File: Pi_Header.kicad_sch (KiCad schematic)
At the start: 31 parts, among them J1 Raspberry_Pi_2_3, J2 UART, J3 I2C, J4 Power_IN, U1 BD9F800MUX-ZE2

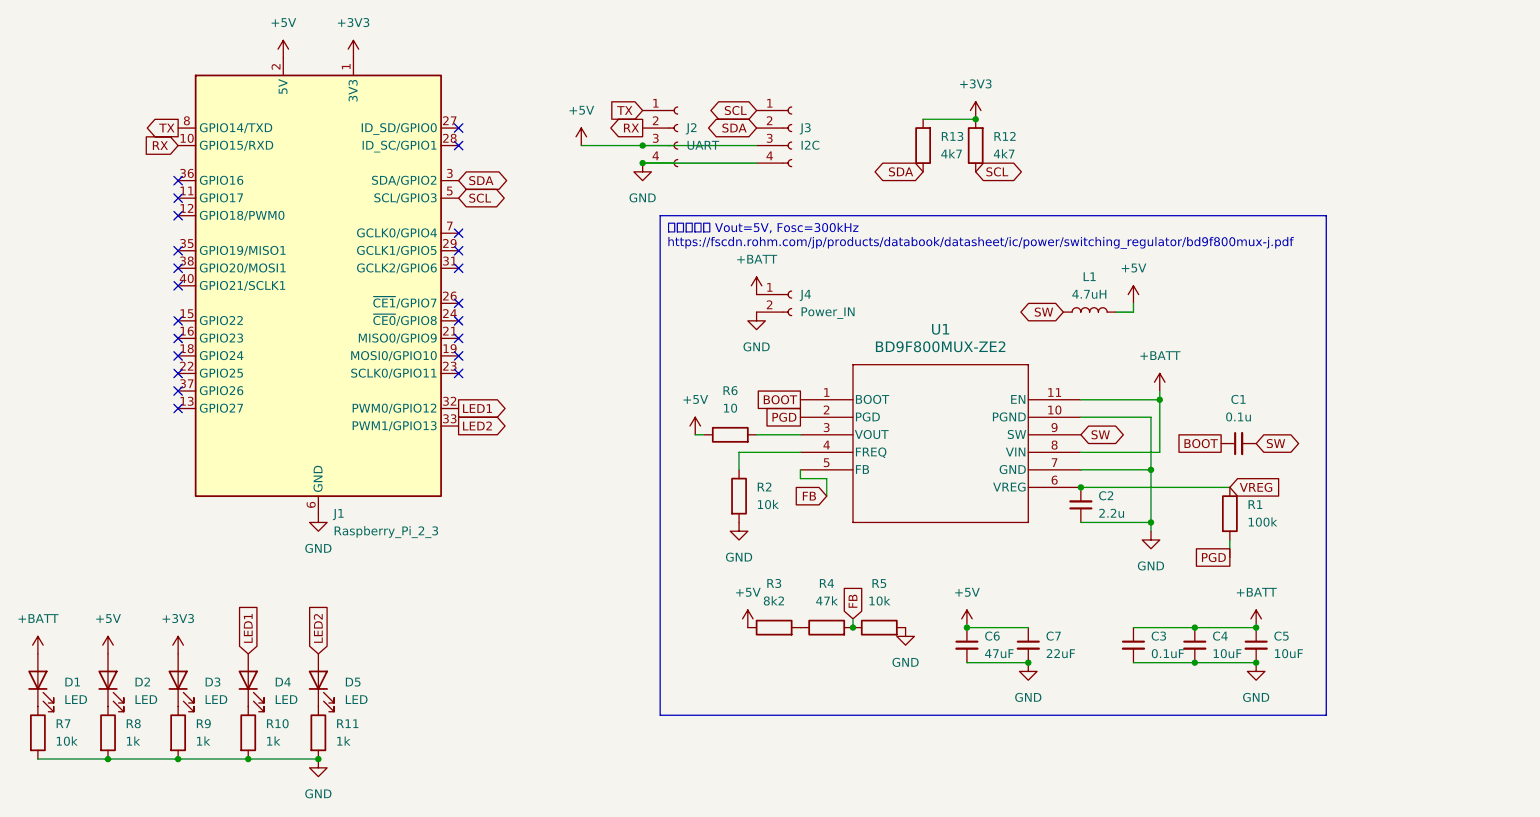
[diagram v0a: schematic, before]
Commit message: スケッチ完成、PCBベタまで完成　あと外形
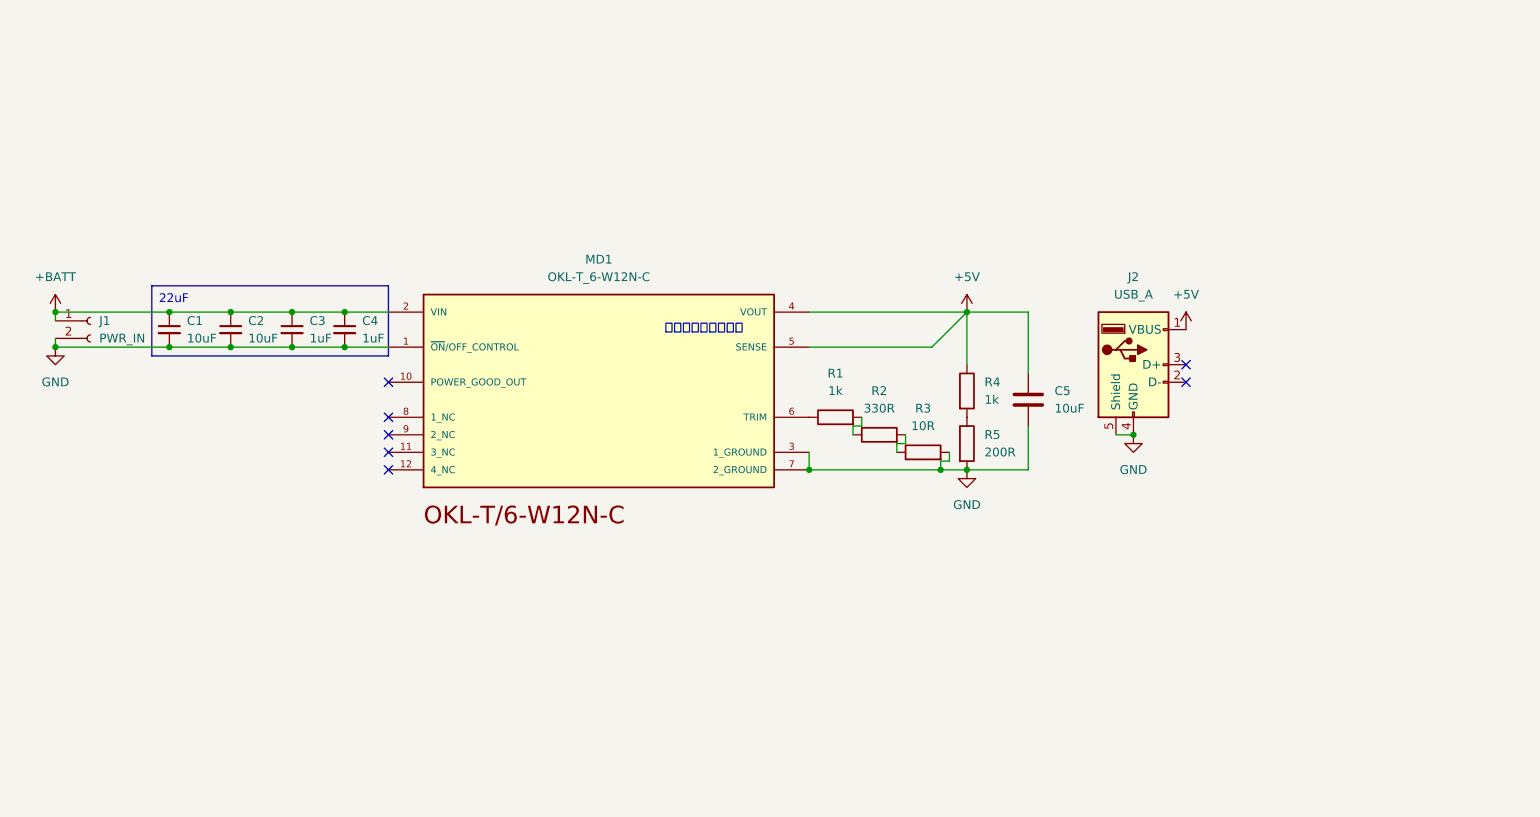
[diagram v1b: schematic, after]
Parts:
- removed C5: 10uF, symbol Device:C_Small
- removed C6: 47uF, symbol Device:C_Small
- removed C7: 22uF, symbol Device:C_Small
- removed D1, D2, D3, D4, D5: LED, symbol Device:LED
- removed J1: Raspberry_Pi_2_3, Connector_IDC:IDC-Header_2x20_P2.54mm_Vertical, symbol Connector:Raspberry_Pi_2_3
- removed J2: UART, Connector_JST:JST_XA_B04B-XASK-1_1x04_P2.50mm_Vertical, symbol Connector:Conn_01x04_Socket
- removed J3: I2C, Connector_JST:JST_XA_B04B-XASK-1_1x04_P2.50mm_Vertical, symbol Connector:Conn_01x04_Socket
- removed J4: Power_IN, symbol Connector:Conn_01x02_Socket
- removed L1: 4.7uH, symbol Device:L
- removed R10, R11, R8, R9: 1k, symbol Device:R
- removed R12, R13: 4k7, symbol Device:R
- removed R6: 10, symbol Device:R
- removed R7: 10k, symbol Device:R
- removed U1: BD9F800MUX-ZE2, VQFN11_ROM:BD9F800MUX, symbol VQFN11_ROM:BD9F800MUX-ZE2
- added C5: 10uF, Capacitor_SMD:C_0805_2012Metric, symbol Device:C
- added J1: PWR_IN, Connector_AMASS:AMASS_XT60-M_1x02_P7.20mm_Vertical, symbol Connector:Conn_01x02_Socket
- added J2: USB_A, Connector_USB:USB_A_CONNFLY_DS1095-WNR0, symbol Connector:USB_A
- added MD1: OKL-T_6-W12N-C, Pi_Header:MURATA_OKL-T-6-W12N-C_0, symbol OKL-T_6-W12N-C:OKL-T_6-W12N-C
- C1: value 0.1u -> 10uF; footprint (none) -> Capacitor_SMD:C_0805_2012Metric
- C2: value 2.2u -> 10uF; footprint (none) -> Capacitor_SMD:C_0805_2012Metric
- C3: value 0.1uF -> 1uF; footprint (none) -> Capacitor_SMD:C_0805_2012Metric
- C4: value 10uF -> 1uF; footprint (none) -> Capacitor_SMD:C_0805_2012Metric
- R1: value 100k -> 1k; footprint (none) -> Resistor_SMD:R_0805_2012Metric
- R2: value 10k -> 330R; footprint (none) -> Resistor_SMD:R_0805_2012Metric
- R3: value 8k2 -> 10R; footprint (none) -> Resistor_SMD:R_0805_2012Metric
- R4: value 47k -> 1k; footprint (none) -> Resistor_SMD:R_0805_2012Metric
- R5: value 10k -> 200R; footprint (none) -> Resistor_SMD:R_0805_2012Metric
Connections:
- net BOOT is gone; now on net +BATT: C1.1
- net PGD is gone; now on an unnamed net: R1.2
- net SW is gone; now on net GND: C1.2
- net +5V: now also R4.1, C5.1, J2.1 (VBUS), MD1.4 (VOUT), MD1.5 (SENSE); no longer R3.1
- net +BATT: now also C2.1, J1.1 (Pin_1), MD1.2 (VIN)
- net GND: now also C2.2, R3.2, C5.2, J1.2 (Pin_2), J2.4 (GND), J2.5 (Shield), MD1.1 (~{ON}/OFF_CONTROL), MD1.3 (1_GROUND), MD1.7 (2_GROUND); no longer C2.1, R2.2
- net FB: no longer names the net of R4.2, R5.1
- net VREG: no longer names the net of R1.1
- net VREG: now also MD1.6 (TRIM); no longer C2.2
- new net: R2.2, R3.1
- no-connect marks 22 -> 7
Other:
- note added: "負荷点付近で接続？"
